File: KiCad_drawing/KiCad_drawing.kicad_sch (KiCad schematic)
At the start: 0 parts

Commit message: base
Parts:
- added U1: ESP32-S2-WROVER, RF_Module:ESP32-S2-WROVER, symbol RF_Module:ESP32-S2-WROVER
- added U2: CR2013-MI2120, Display:CR2013-MI2120, symbol Driver_Display:CR2013-MI2120
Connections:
- new net: U1.1 (GND), U1.26 (GND), U1.42 (GND), U1.43 (GND)
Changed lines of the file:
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@@
 	(generator_version "9.0")
 	(paper "A4")
+	(symbol
+		(lib_id "Driver_Display:CR2013-MI2120")
+		(at 81.28 57.15 0)
+		(unit 1)
+		(exclude_from_sim no)
+		(in_bom yes)
+		(on_board yes)
+		(dnp no)
+		(fields_autoplaced yes)
+		(property "Reference" "U2"
+			(at 83.4233 39.37 0)
+			(effects
+				(font
+					(size 1.27 1.27)
+				)
+				(justify left)
+			)
+		)
+		(property "Value" "CR2013-MI2120"
+			(at 83.4233 41.91 0)
+			(effects
+				(font
+					(size 1.27 1.27)
+				)
+				(justify left)
+			)
+		)
+		(property "Footprint" "Display:CR2013-MI2120"
+			(at 81.28 74.93 0)
+			(effects
+				(font
+					(size 1.27 1.27)
+				)
+				(hide yes)
+			)
+		)
+		(property "Datasheet" "http://pan.baidu.com/s/11Y990"
+			(at 64.77 44.45 0)
+			(effects
+				(font
+					(size 1.27 1.27)
+				)
+				(hide yes)
+			)
+		)
+		(property "Description" "ILI9341 controller, SPI TFT LCD Display, 9-pin breakout PCB, 4-pin SD card interface, 5V/3.3V"
+			(at 81.28 57.15 0)
+			(effects
+				(font
+					(size 1.27 1.27)
+				)
+				(hide yes)
+			)
+		)
+		(pin "10"
+		)
+		(pin "11"
+		)
+		(pin "12"
+		)
+		(pin "6"
+		)
+		(pin "5"
+		)
+		(pin "1"
+		)
+		(pin "2"
+		)
+		(pin "14"
+		)
+		(pin "3"
+		)
+		(pin "13"
+		)
+		(pin "9"
+		)
+		(pin "7"
+		)
+		(pin "4"
+		)
+		(pin "8"
+		)
+		(instances
+			(project ""
+				(path "/84f52bee-438a-4d9d-954b-8743e5ddad6b"
+					(reference "U2")
+					(unit 1)
+				)
+			)
+		)
+	)
+	(symbol
+		(lib_id "RF_Module:ESP32-S2-WROVER")
+		(at 140.97 93.98 0)
+		(unit 1)
+		(exclude_from_sim no)
+		(in_bom yes)
+		(on_board yes)
+		(dnp no)
+		(fields_autoplaced yes)
+		(property "Reference" "U1"
+			(at 143.1133 60.96 0)
+			(effects
+				(font
+					(size 1.27 1.27)
+				)
+				(justify left)
+			)
+		)
+		(property "Value" "ESP32-S2-WROVER"
+			(at 143.1133 63.5 0)
+			(effects
+				(font
+					(size 1.27 1.27)
+				)
+				(justify left)
+			)
+		)
+		(property "Footprint" "RF_Module:ESP32-S2-WROVER"
+			(at 160.02 123.19 0)
+			(effects
+				(font
+					(size 1.27 1.27)
+				)
+				(hide yes)
+			)
+		)
+		(property "Datasheet" "https://www.espressif.com/sites/default/files/documentation/esp32-s2-wroom_esp32-s2-wroom-i_datasheet_en.pdf"
+			(at 133.35 114.3 0)
+			(effects
+				(font
+					(size 1.27 1.27)
+				)
+				(hide yes)
+			)
+		)
+		(property "Description" "RF Module, ESP32-D0WDQ6 SoC, Wi-Fi 802.11b/g/n, 32-bit, 2.7-3.6V, onboard antenna, SMD"
+			(at 140.97 93.98 0)
+			(effects
+				(font
+					(size 1.27 1.27)
+				)
+				(hide yes)
+			)
+		)
+		(pin "5"
+		)
+		(pin "10"
+		)
+		(pin "40"
+		)
+		(pin "2"
+		)
+		(pin "19"
+		)
+		(pin "1"
+		)
+		(pin "3"
+		)
+		(pin "41"
+		)
+		(pin "15"
+		)
+		(pin "32"
+		)
+		(pin "6"
+		)
+		(pin "26"
+		)
+		(pin "11"
+		)
+		(pin "17"
+		)
+		(pin "13"
+		)
+		(pin "18"
+		)
+		(pin "42"
+		)
+		(pin "43"
+		)
+		(pin "14"
+		)
+		(pin "4"
+		)
+		(pin "9"
+		)
+		(pin "20"
+		)
+		(pin "7"
+		)
+		(pin "8"
+		)
+		(pin "21"
+		)
+		(pin "16"
+		)
+		(pin "12"
+		)
+		(pin "39"
+		)
+		(pin "38"
+		)
+		(pin "36"
+		)
+		(pin "35"
+		)
+		(pin "34"
+		)
+		(pin "33"
+		)
+		(pin "37"
+		)
+		(pin "30"
+		)
+		(pin "29"
+		)
+		(pin "28"
+		)
+		(pin "25"
+		)
+		(pin "24"
+		)
+		(pin "27"
+		)
+		(pin "23"
+		)
+		(pin "31"
+		)
+		(pin "22"
+		)
+		(instances
+			(project ""
+				(path "/84f52bee-438a-4d9d-954b-8743e5ddad6b"
+					(reference "U1")
+					(unit 1)
+				)
+			)
+		)
+	)
 	(sheet_instances
 		(path "/"

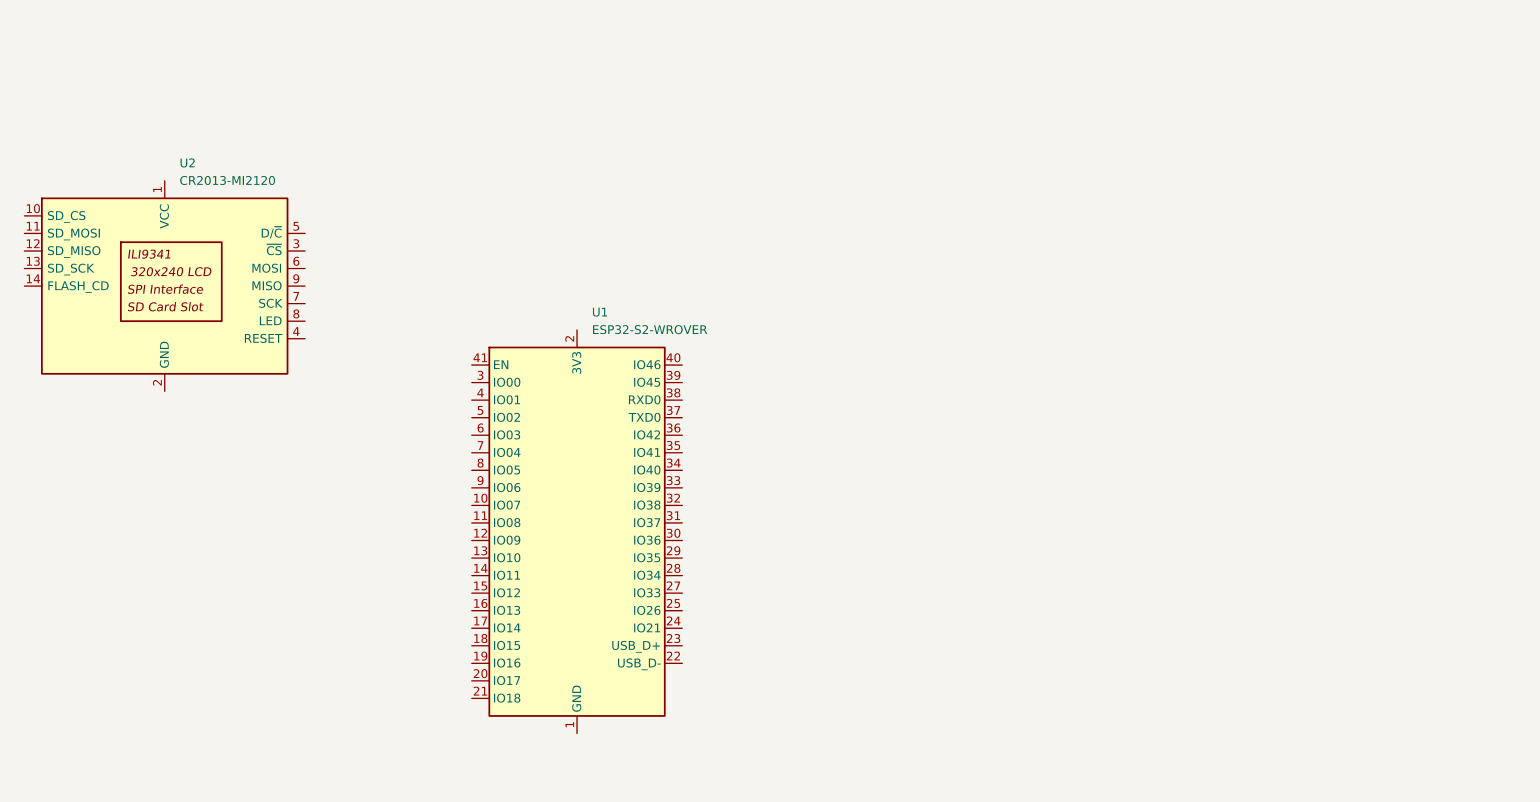
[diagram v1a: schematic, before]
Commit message: Add debug macros and update KiCad symbols
Introduced DEBUG macros for conditional serial output in GG_star_fighter.ino and replaced direct Serial prints with debug macros. Updated KiCad schematic to replace display and ESP32 symbols with MAX98357B audio DAC, AP9101CK battery protection, and LTC4055 charger symbols, including pinout and metadata changes. Added new KiCad backup files and updated project settings for net inspector and board design.
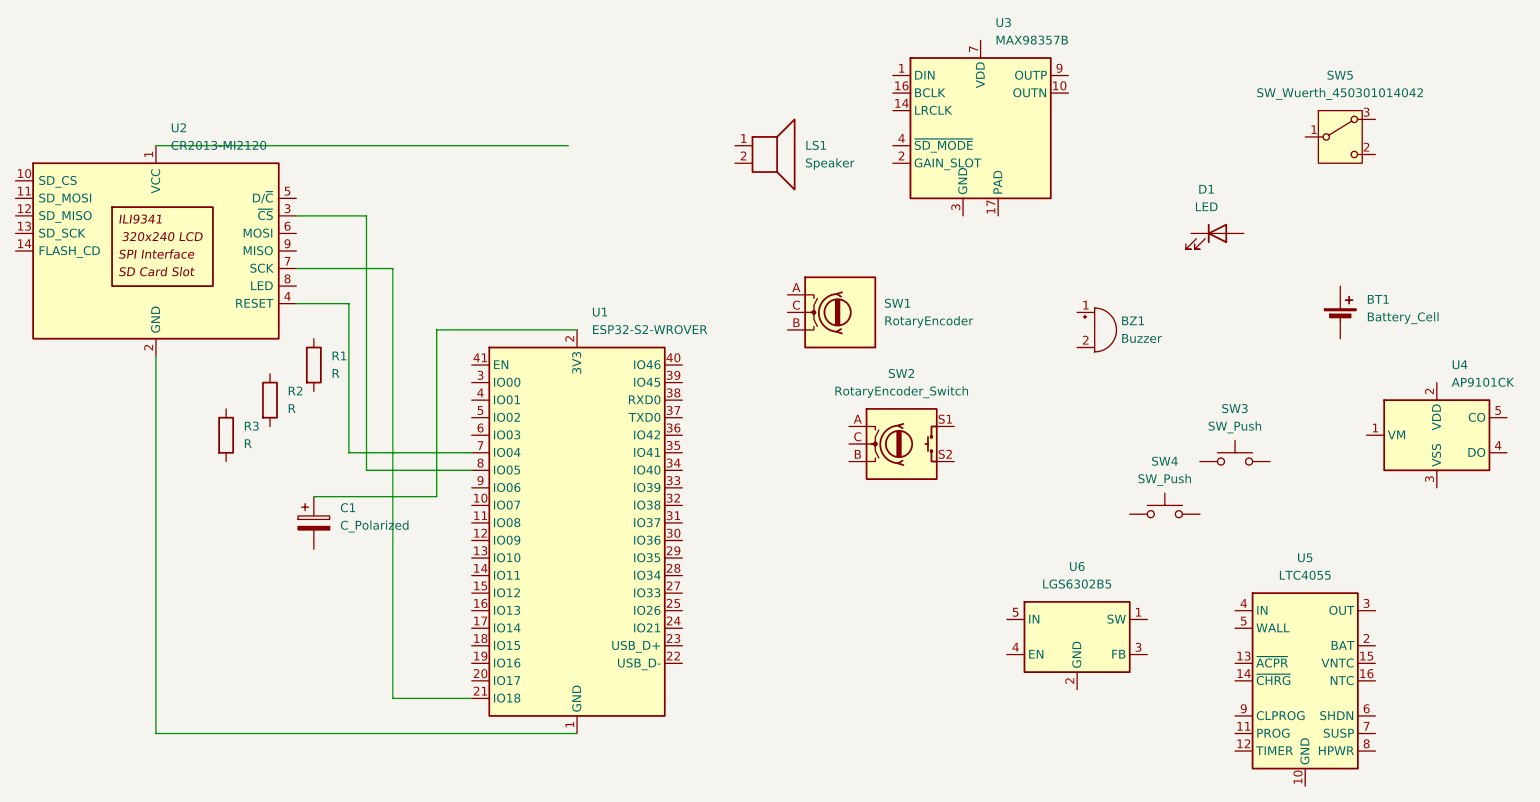
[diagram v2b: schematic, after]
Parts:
- added BT1: Battery_Cell, symbol Device:Battery_Cell
- added BZ1: Buzzer, symbol Device:Buzzer
- added C1: C_Polarized, symbol Device:C_Polarized
- added D1: LED, symbol Device:LED
- added LS1: Speaker, symbol Device:Speaker
- added R1, R2, R3: R, symbol Device:R
- added SW1: RotaryEncoder, symbol Device:RotaryEncoder
- added SW2: RotaryEncoder_Switch, symbol Device:RotaryEncoder_Switch
- added SW3, SW4: SW_Push, symbol Switch:SW_Push
- added SW5: SW_Wuerth_450301014042, Button_Switch_THT:SW_Slide-03_Wuerth-WS-SLTV_10x2.5x6.4_P2.54mm, symbol Switch:SW_Wuerth_450301014042
- added U3: MAX98357B, Package_DFN_QFN:TQFN-16-1EP_3x3mm_P0.5mm_EP1.23x1.23mm, symbol Audio:MAX98357B
- added U4: AP9101CK, Package_TO_SOT_SMD:SOT-23-5, symbol Battery_Management:AP9101CK
- added U5: LTC4055, Package_DFN_QFN:QFN-16-1EP_4x4mm_P0.65mm_EP2.15x2.15mm, symbol Battery_Management:LTC4055
- added U6: LGS6302B5, Package_TO_SOT_SMD:SOT-23-5, symbol Regulator_Switching:LGS6302B5
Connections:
- net at U2.2 (GND): now also U1.1 (GND), U1.26 (GND), U1.42 (GND), U1.43 (GND)
- net at U2.3 (~{CS}): now also U1.8 (IO05)
- net at U2.4 (RESET): now also U1.7 (IO04)
- net at U2.7 (SCK): now also U1.21 (IO18)
- net at U1.2 (3V3): now also C1.1
- new net: U3.11 (GND), U3.15 (GND), U3.3 (GND)
- new net: U3.7 (VDD), U3.8 (VDD)
- new net: U5.1 (IN), U5.4 (IN)
- new net: U5.10 (GND), U5.17 (GND)
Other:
- moved on the sheet: U2
